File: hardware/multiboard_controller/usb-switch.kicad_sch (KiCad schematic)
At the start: 1 part, among them U1 max4999etj+

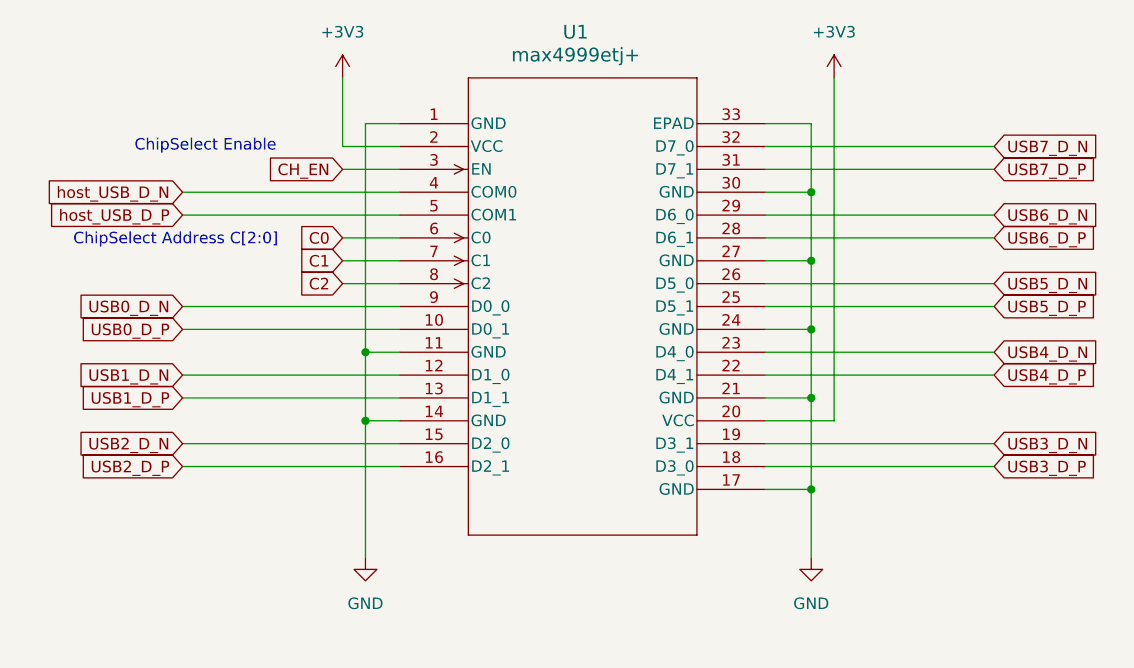
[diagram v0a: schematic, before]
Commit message: Add Channel Select switches and USB output ports
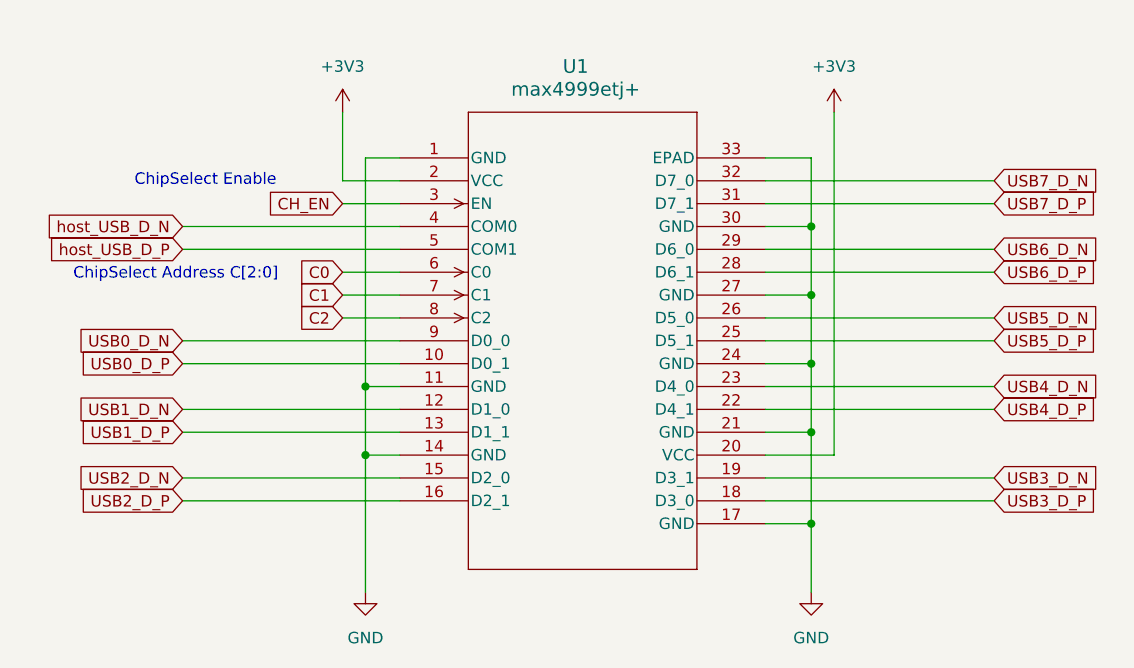
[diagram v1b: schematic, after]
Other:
- moved on the sheet: U1
